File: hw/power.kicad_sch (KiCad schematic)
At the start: 7 parts, among them Q1 PMH550UPE, U7 NCP167

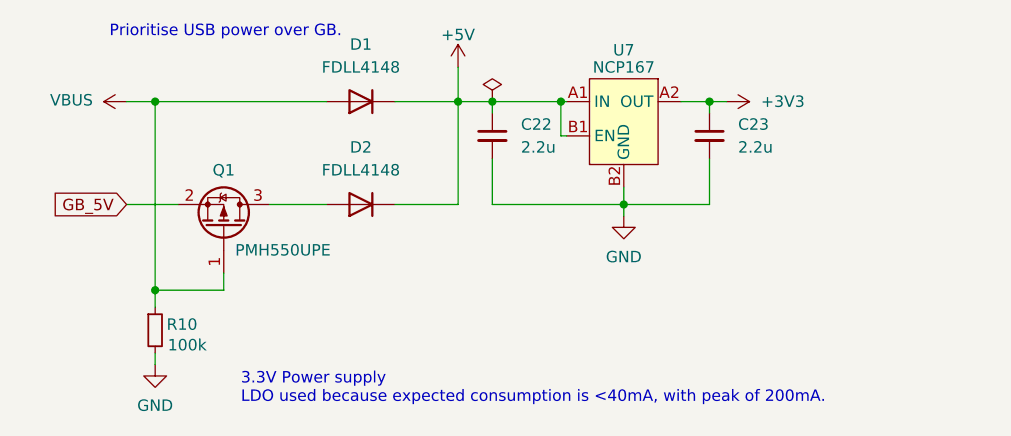
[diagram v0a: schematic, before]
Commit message: hw: use parts from LCSC
Signed-off-by: Mahyar Koshkouei <mk@deltabeard.com>
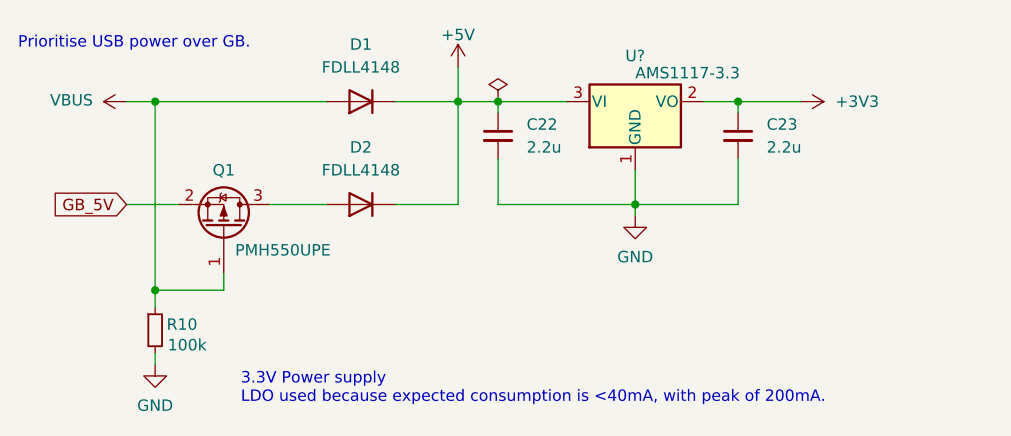
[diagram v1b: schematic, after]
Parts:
- removed U7: NCP167, Project_Specific:WLCSP-4-0.64x0.64mm_P0.35mm, symbol Project_specific:NCP167
- added U?: AMS1117-3.3, Package_TO_SOT_SMD:SOT-223-3_TabPin2, symbol Regulator_Linear:AMS1117-3.3
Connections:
- net +3V3: now also U?.2 (VO)
- net +5V: now also U?.3 (VI)
- net GND: now also U?.1 (GND)
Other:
- moved on the sheet: C22, C23

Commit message: hw: complete 2-layer PCB
Signed-off-by: Mahyar Koshkouei <mk@deltabeard.com>
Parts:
- removed C23: 2.2u, Capacitor_SMD:C_0603_1608Metric, symbol Device:C_Small
- removed D1, D2: FDLL4148, Diode_SMD:D_MiniMELF, symbol Diode:1N4149
- added C22: 100u, Capacitor_Tantalum_SMD:CP_EIA-3528-15_AVX-H, symbol Device:C_Polarized_Small
- added D1: D_Dual_CommonCathode_AAK_Split, Package_TO_SOT_SMD:SOT-23, symbol Device:D_Dual_CommonCathode_AAK_Split
- C21: renamed from C22; LCSC (none) -> C23630
- Q1: value PMH550UPE -> SI2301CDS-T1-GE3; footprint Project_Specific:DFN0606-3 -> Package_TO_SOT_SMD:SOT-23; LCSC (none) -> C10487
- R8: renamed from R10; LCSC (none) -> C25803
- U7: renamed from U?; LCSC C426566 -> C6186
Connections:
- net +3V3: now also C22.1
- net +5V: now also D1.3 (K)
- net GND: now also C22.2
- net VBUS: now also D1.1 (A)
- net at Q1.3 (D): now also D1.2 (K)
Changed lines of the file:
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@@
   (symbol (lib_id "power:VBUS") (at 113.665 77.47 90) (unit 1)
     (in_bom yes) (on_board yes)
-    (property "Reference" "#PWR049" (id 0) (at 117.475 77.47 0)
+    (property "Reference" "#PWR044" (id 0) (at 117.475 77.47 0)
       (effects (font (size 1.27 1.27)) hide)
     )
@@
   (symbol (lib_id "power:+5V") (at 150.495 73.66 0) (unit 1)
     (in_bom yes) (on_board yes) (fields_autoplaced)
-    (property "Reference" "#PWR051" (id 0) (at 150.495 77.47 0)
+    (property "Reference" "#PWR046" (id 0) (at 150.495 77.47 0)
       (effects (font (size 1.27 1.27)) hide)
     )
@@
   (symbol (lib_id "power:+3V3") (at 188.595 77.47 270) (unit 1)
     (in_bom yes) (on_board yes) (fields_autoplaced)
-    (property "Reference" "#PWR053" (id 0) (at 184.785 77.47 0)
+    (property "Reference" "#PWR048" (id 0) (at 184.785 77.47 0)
       (effects (font (size 1.27 1.27)) hide)
     )
@@
   (symbol (lib_id "power:GND") (at 116.84 106.68 0) (unit 1)
     (in_bom yes) (on_board yes) (fields_autoplaced)
-    (property "Reference" "#PWR050" (id 0) (at 116.84 113.03 0)
+    (property "Reference" "#PWR045" (id 0) (at 116.84 113.03 0)
       (effects (font (size 1.27 1.27)) hide)
     )
@@
   (symbol (lib_id "power:GND") (at 170.18 90.17 0) (unit 1)
     (in_bom yes) (on_board yes) (fields_autoplaced)
-    (property "Reference" "#PWR052" (id 0) (at 170.18 96.52 0)
+    (property "Reference" "#PWR047" (id 0) (at 170.18 96.52 0)
       (effects (font (size 1.27 1.27)) hide)
     )
@@
   (symbol (lib_id "Device:R_Small") (at 116.84 102.87 0) (unit 1)
     (in_bom yes) (on_board yes)
-    (property "Reference" "R10" (id 0) (at 118.11 102.2349 0)
+    (property "Reference" "R8" (id 0) (at 118.11 102.2349 0)
       (effects (font (size 1.27 1.27)) (justify left))
     )
@@
       (effects (font (size 1.27 1.27)) hide)
     )
+    (property "LCSC" "C25803" (id 4) (at 116.84 102.87 0)
+      (effects (font (size 1.27 1.27)) hide)
+    )
+    (pin "1")
+    (pin "2")
+  )
+  (symbol (lib_id "Device:C_Polarized_Small") (at 181.61 81.28 0) (unit 1)
+    (in_bom yes) (on_board yes) (fields_autoplaced)
+    (property "Reference" "C22" (id 0) (at 184.15 81.2799 0)
+      (effects (font (size 1.27 1.27)) (justify left))
+    )
+    (property "Value" "100u" (id 1) (at 181.864 83.312 0)
+      (effects (font (size 1.27 1.27)) (justify left))
+    )
+    (property "Footprint" "Capacitor_Tantalum_SMD:CP_EIA-3528-15_AVX-H" (id 2) (at 181.61 81.28 0)
+      (effects (font (size 1.27 1.27)) hide)
+    )
+    (property "Datasheet" "~" (id 3) (at 181.61 81.28 0)
+      (effects (font (size 1.27 1.27)) hide)
+    )
+    (property "LCSC" "C16133" (id 4) (at 181.61 81.28 0)
+      (effects (font (size 1.27 1.27)) hide)
+    )
     (pin "1")
     (pin "2")
@@
   (symbol (lib_id "Device:C_Small") (at 154.94 81.28 0) (unit 1)
     (in_bom yes) (on_board yes) (fields_autoplaced)
-    (property "Reference" "C22" (id 0) (at 158.115 80.0099 0)
+    (property "Reference" "C21" (id 0) (at 158.115 80.0099 0)
       (effects (font (size 1.27 1.27)) (justify left))
     )
@@
       (effects (font (size 1.27 1.27)) hide)
     )
-    (pin "1")
-    (pin "2")
-  )
-  (symbol (lib_id "Device:C_Small") (at 181.61 81.28 0) (unit 1)
-    (in_bom yes) (on_board yes) (fields_autoplaced)
-    (property "Reference" "C23" (id 0) (at 184.785 80.0099 0)
-      (effects (font (size 1.27 1.27)) (justify left))
-    )
-    (property "Value" "2.2u" (id 1) (at 184.785 82.5499 0)
-      (effects (font (size 1.27 1.27)) (justify left))
-    )
-    (property "Footprint" "Capacitor_SMD:C_0603_1608Metric" (id 2) (at 181.61 81.28 0)
-      (effects (font (size 1.27 1.27)) hide)
-    )
-    (property "Datasheet" "~" (id 3) (at 181.61 81.28 0)
-      (effects (font (size 1.27 1.27)) hide)
-    )
-    (pin "1")
-    (pin "2")
-  )
-  (symbol (lib_id "Diode:1N4149") (at 139.7 77.47 180) (unit 1)
-    (in_bom yes) (on_board yes) (fields_autoplaced)
-    (property "Reference" "D1" (id 0) (at 139.7 71.12 0))
-    (property "Value" "FDLL4148" (id 1) (at 139.7 73.66 0))
-    (property "Footprint" "Diode_SMD:D_MiniMELF" (id 2) (at 139.7 73.025 0)
-      (effects (font (size 1.27 1.27)) hide)
-    )
-    (property "Datasheet" "http://www.microsemi.com/document-portal/doc_view/11580-lds-0239" (id 3) (at 139.7 77.47 0)
-      (effects (font (size 1.27 1.27)) hide)
-    )
-    (pin "1")
-    (pin "2")
-  )
-  (symbol (lib_id "Diode:1N4149") (at 139.7 88.9 180) (unit 1)
-    (in_bom yes) (on_board yes) (fields_autoplaced)
-    (property "Reference" "D2" (id 0) (at 139.7 82.55 0))
-    (property "Value" "FDLL4148" (id 1) (at 139.7 85.09 0))
-    (property "Footprint" "Diode_SMD:D_MiniMELF" (id 2) (at 139.7 84.455 0)
-      (effects (font (size 1.27 1.27)) hide)
-    )
-    (property "Datasheet" "http://www.microsemi.com/document-portal/doc_view/11580-lds-0239" (id 3) (at 139.7 88.9 0)
-      (effects (font (size 1.27 1.27)) hide)
-    )
-    (pin "1")
+    (property "LCSC" "C23630" (id 4) (at 154.94 81.28 0)
+      (effects (font (size 1.27 1.27)) hide)
+    )
+    (pin "1")
+    (pin "2")
+  )
+  (symbol (lib_id "Device:D_Dual_CommonCathode_AAK_Split") (at 139.7 77.47 0) (unit 1)
+    (in_bom yes) (on_board yes) (fields_autoplaced)
+    (property "Reference" "D1" (id 0) (at 139.7 73.025 0))
+    (property "Value" "D_Dual_CommonCathode_AAK_Split" (id 1) (at 139.7 80.01 0))
+    (property "Footprint" "Package_TO_SOT_SMD:SOT-23" (id 2) (at 137.16 80.01 0)
+      (effects (font (size 1.27 1.27)) hide)
+    )
+    (property "Datasheet" "~" (id 3) (at 137.16 80.01 0)
+      (effects (font (size 1.27 1.27)) hide)
+    )
+    (property "LCSC" "C68978" (id 4) (at 139.7 77.47 0)
+      (effects (font (size 1.27 1.27)) hide)
+    )
+    (property "MFr" "BAV70" (id 5) (at 139.7 77.47 0)
+      (effects (font (size 1.27 1.27)) hide)
+    )
+    (pin "1")
+    (pin "3")
+  )
+  (symbol (lib_id "Device:D_Dual_CommonCathode_AAK_Split") (at 139.7 88.9 0) (unit 2)
+    (in_bom yes) (on_board yes)
+    (property "Reference" "D1" (id 0) (at 137.795 85.1582 0)
+      (effects (font (size 1.27 1.27)) (justify left))
+    )
+    (property "Value" "D_Dual_CommonCathode_AAK_Split" (id 1) (at 139.7 91.44 0))
+    (property "Footprint" "Package_TO_SOT_SMD:SOT-23" (id 2) (at 137.16 91.44 0)
+      (effects (font (size 1.27 1.27)) hide)
+    )
+    (property "Datasheet" "~" (id 3) (at 137.16 91.44 0)
+      (effects (font (size 1.27 1.27)) hide)
+    )
+    (property "LCSC" "C68978" (id 4) (at 139.7 88.9 0)
+      (effects (font (size 1.27 1.27)) hide)
+    )
+    (property "MFr" "BAV70" (id 5) (at 139.7 88.9 0)
+      (effects (font (size 1.27 1.27)) hide)
+    )
     (pin "2")
   )
@@
     (in_bom yes) (on_board yes)
     (property "Reference" "Q1" (id 0) (at 124.46 85.09 90))
-    (property "Value" "PMH550UPE" (id 1) (at 125.73 93.98 90)
-      (effects (font (size 1.27 1.27)) (justify left))
-    )
-    (property "Footprint" "Project_Specific:DFN0606-3" (id 2) (at 122.555 86.36 0)
+    (property "Value" "SI2301CDS-T1-GE3" (id 1) (at 125.73 93.98 90)
+      (effects (font (size 1.27 1.27)) (justify left))
+    )
+    (property "Footprint" "Package_TO_SOT_SMD:SOT-23" (id 2) (at 122.555 86.36 0)
       (effects (font (size 1.27 1.27) italic) (justify left) hide)
     )
-    (property "Datasheet" "https://www.mouser.co.uk/datasheet/2/916/PMH550UPE-1839916.pdf" (id 3) (at 124.46 91.44 0)
+    (property "Datasheet" "https://datasheet.lcsc.com/lcsc/1807281741_ROHM-Semicon-RZF020P01TL_C253530.pdf" (id 3) (at 124.46 91.44 0)
       (effects (font (size 1.27 1.27)) (justify left) hide)
     )
+    (property "LCSC" "C10487" (id 4) (at 124.46 91.44 0)
+      (effects (font (size 1.27 1.27)) hide)
+    )
     (pin "1")
     (pin "2")
@@
   (symbol (lib_id "Regulator_Linear:AMS1117-3.3") (at 170.18 77.47 0) (unit 1)
     (in_bom yes) (on_board yes) (fields_autoplaced)
-    (property "Reference" "U?" (id 0) (at 170.18 72.39 0))
+    (property "Reference" "U7" (id 0) (at 170.18 72.39 0))
     (property "Value" "AMS1117-3.3" (id 1) (at 170.18 74.295 0)
       (effects (font (size 1.27 1.27)) (justify left))
@@
       (effects (font (size 1.27 1.27)) hide)
     )
-    (property "LCSC" "C426566" (id 4) (at 170.18 77.47 0)
-      (effects (font (size 1.27 1.27)) hide)
-    )
+    (property "LCSC" "C6186" (id 4) (at 170.18 77.47 0)
+      (effects (font (size 1.27 1.27)) hide)
+    )

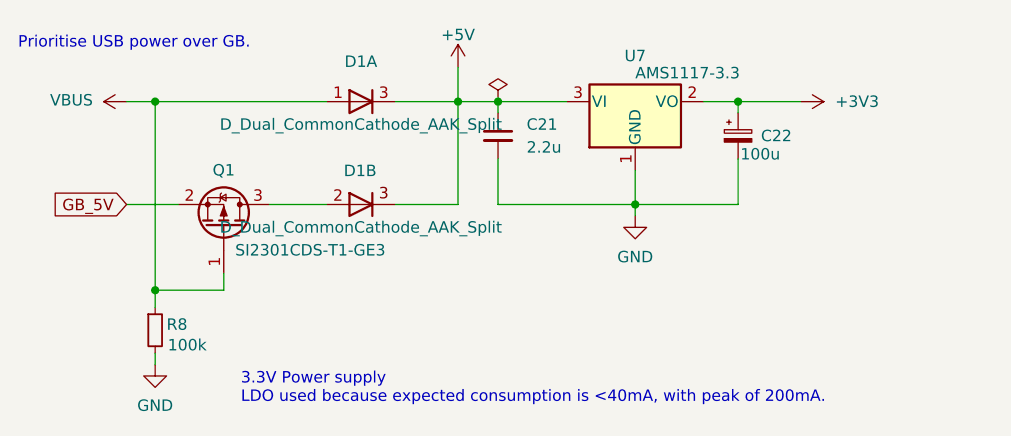
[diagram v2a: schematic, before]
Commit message: hw: complete routing
Use components available on LCSC.

Signed-off-by: Mahyar Koshkouei <mk@deltabeard.com>
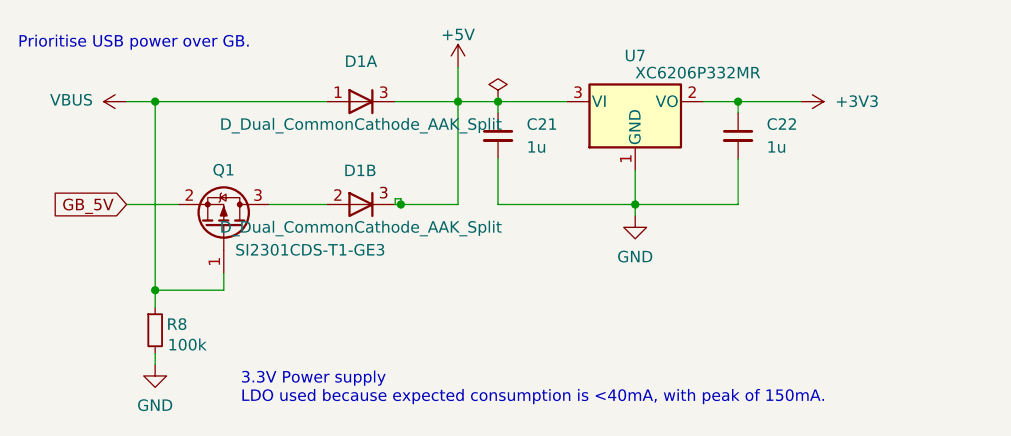
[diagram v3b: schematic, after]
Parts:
- removed C22: 100u, Capacitor_Tantalum_SMD:CP_EIA-3528-15_AVX-H, symbol Device:C_Polarized_Small
- added C22: 1u, Capacitor_SMD:C_0603_1608Metric, symbol Device:C_Small
- C21: value 2.2u -> 1u; LCSC C23630 -> C15849
- U7: value AMS1117-3.3 -> XC6206P332MR; footprint Package_TO_SOT_SMD:SOT-223-3_TabPin2 -> Package_TO_SOT_SMD:SOT-23; LCSC C6186 -> C5446
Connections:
- net +3V3: now also C22.1
- net GND: now also C22.2
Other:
- note added: "3.3V Power supply LDO used because expected consumption is <40mA, with peak of 150mA."
- note removed: "3.3V Power supply LDO used because expected consumption is <40mA, with peak of 200mA."
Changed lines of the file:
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@@
   (junction (at 116.84 77.47) (diameter 0.9144) (color 0 0 0 0))
   (junction (at 116.84 98.425) (diameter 0.9144) (color 0 0 0 0))
+  (junction (at 144.145 88.9) (diameter 0.9144) (color 0 0 0 0))
   (junction (at 150.495 77.47) (diameter 0.9144) (color 0 0 0 0))
   (junction (at 154.94 77.47) (diameter 0.9144) (color 0 0 0 0))
@@
     (stroke (width 0) (type solid) (color 0 0 0 0))
   )
-  (wire (pts (xy 143.51 88.9) (xy 150.495 88.9))
+  (wire (pts (xy 143.51 88.265) (xy 144.145 88.265))
+    (stroke (width 0) (type solid) (color 0 0 0 0))
+  )
+  (wire (pts (xy 143.51 88.9) (xy 143.51 88.265))
+    (stroke (width 0) (type solid) (color 0 0 0 0))
+  )
+  (wire (pts (xy 143.51 88.9) (xy 144.145 88.9))
+    (stroke (width 0) (type solid) (color 0 0 0 0))
+  )
+  (wire (pts (xy 144.145 88.265) (xy 144.145 88.9))
+    (stroke (width 0) (type solid) (color 0 0 0 0))
+  )
+  (wire (pts (xy 144.145 88.9) (xy 150.495 88.9))
     (stroke (width 0) (type solid) (color 0 0 0 0))
   )
@@
     (effects (font (size 1.27 1.27)) (justify left bottom))
   )
-  (text "3.3V Power supply\nLDO used because expected consumption is <40mA, with peak of 200mA."
+  (text "3.3V Power supply\nLDO used because expected consumption is <40mA, with peak of 150mA."
     (at 126.365 111.125 0)
     (effects (font (size 1.27 1.27)) (justify left bottom))
@@
     (pin "2")
   )
-  (symbol (lib_id "Device:C_Polarized_Small") (at 181.61 81.28 0) (unit 1)
-    (in_bom yes) (on_board yes) (fields_autoplaced)
-    (property "Reference" "C22" (id 0) (at 184.15 81.2799 0)
-      (effects (font (size 1.27 1.27)) (justify left))
-    )
-    (property "Value" "100u" (id 1) (at 181.864 83.312 0)
-      (effects (font (size 1.27 1.27)) (justify left))
-    )
-    (property "Footprint" "Capacitor_Tantalum_SMD:CP_EIA-3528-15_AVX-H" (id 2) (at 181.61 81.28 0)
+  (symbol (lib_id "Device:C_Small") (at 154.94 81.28 0) (unit 1)
+    (in_bom yes) (on_board yes) (fields_autoplaced)
+    (property "Reference" "C21" (id 0) (at 158.115 80.0099 0)
+      (effects (font (size 1.27 1.27)) (justify left))
+    )
+    (property "Value" "1u" (id 1) (at 158.115 82.5499 0)
+      (effects (font (size 1.27 1.27)) (justify left))
+    )
+    (property "Footprint" "Capacitor_SMD:C_0603_1608Metric" (id 2) (at 154.94 81.28 0)
+      (effects (font (size 1.27 1.27)) hide)
+    )
+    (property "Datasheet" "~" (id 3) (at 154.94 81.28 0)
+      (effects (font (size 1.27 1.27)) hide)
+    )
+    (property "LCSC" "C15849" (id 4) (at 154.94 81.28 0)
+      (effects (font (size 1.27 1.27)) hide)
+    )
+    (pin "1")
+    (pin "2")
+  )
+  (symbol (lib_id "Device:C_Small") (at 181.61 81.28 0) (unit 1)
+    (in_bom yes) (on_board yes) (fields_autoplaced)
+    (property "Reference" "C22" (id 0) (at 184.785 80.0099 0)
+      (effects (font (size 1.27 1.27)) (justify left))
+    )
+    (property "Value" "1u" (id 1) (at 184.785 82.5499 0)
+      (effects (font (size 1.27 1.27)) (justify left))
+    )
+    (property "Footprint" "Capacitor_SMD:C_0603_1608Metric" (id 2) (at 181.61 81.28 0)
       (effects (font (size 1.27 1.27)) hide)
     )
@@
       (effects (font (size 1.27 1.27)) hide)
     )
-    (property "LCSC" "C16133" (id 4) (at 181.61 81.28 0)
-      (effects (font (size 1.27 1.27)) hide)
-    )
-    (pin "1")
-    (pin "2")
-  )
-  (symbol (lib_id "Device:C_Small") (at 154.94 81.28 0) (unit 1)
-    (in_bom yes) (on_board yes) (fields_autoplaced)
-    (property "Reference" "C21" (id 0) (at 158.115 80.0099 0)
-      (effects (font (size 1.27 1.27)) (justify left))
-    )
-    (property "Value" "2.2u" (id 1) (at 158.115 82.5499 0)
-      (effects (font (size 1.27 1.27)) (justify left))
-    )
-    (property "Footprint" "Capacitor_SMD:C_0603_1608Metric" (id 2) (at 154.94 81.28 0)
-      (effects (font (size 1.27 1.27)) hide)
-    )
-    (property "Datasheet" "~" (id 3) (at 154.94 81.28 0)
-      (effects (font (size 1.27 1.27)) hide)
-    )
-    (property "LCSC" "C23630" (id 4) (at 154.94 81.28 0)
+    (property "LCSC" "C15849" (id 4) (at 181.61 81.28 0)
       (effects (font (size 1.27 1.27)) hide)
     )
@@
     (in_bom yes) (on_board yes) (fields_autoplaced)
     (property "Reference" "U7" (id 0) (at 170.18 72.39 0))
-    (property "Value" "AMS1117-3.3" (id 1) (at 170.18 74.295 0)
-      (effects (font (size 1.27 1.27)) (justify left))
-    )
-    (property "Footprint" "Package_TO_SOT_SMD:SOT-223-3_TabPin2" (id 2) (at 170.18 72.39 0)
+    (property "Value" "XC6206P332MR" (id 1) (at 170.18 74.295 0)
+      (effects (font (size 1.27 1.27)) (justify left))
+    )
+    (property "Footprint" "Package_TO_SOT_SMD:SOT-23" (id 2) (at 170.18 72.39 0)
       (effects (font (size 1.27 1.27)) hide)
     )
@@
       (effects (font (size 1.27 1.27)) hide)
     )
-    (property "LCSC" "C6186" (id 4) (at 170.18 77.47 0)
-      (effects (font (size 1.27 1.27)) hide)
-    )
+    (property "LCSC" "C5446" (id 4) (at 170.18 77.47 0)
+      (effects (font (size 1.27 1.27)) hide)
+    )
